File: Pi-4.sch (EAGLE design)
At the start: 14 parts, among them IC1 DS18B20, X1 RASPI_GPIO_B+#_PIN, X2 HDD, 5V 700mA, X3 MAC64L

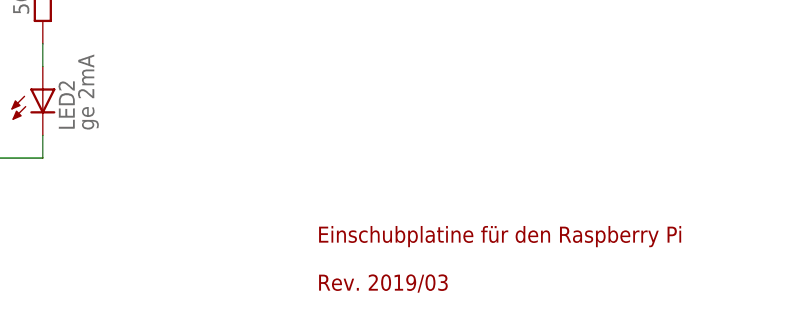
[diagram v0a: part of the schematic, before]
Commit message: Schaltpläne aufgehübscht zur Veröffentlichung
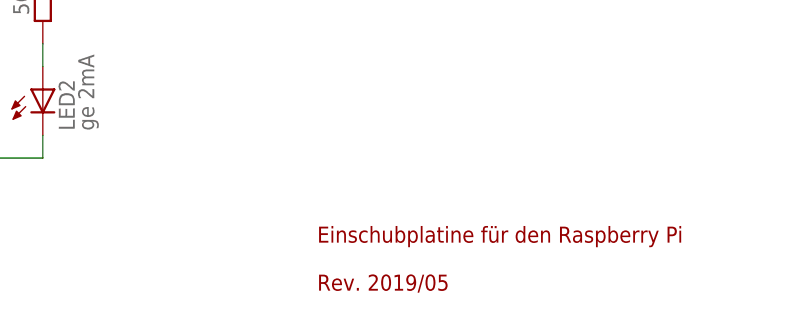
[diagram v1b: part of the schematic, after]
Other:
- note added: "Einschubplatine für den Raspberry Pi Rev. 2019/05"
- note removed: "Einschubplatine für den Raspberry Pi Rev. 2019/03"
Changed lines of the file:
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@@
 <plain>
 <text x="162.56" y="20.32" size="1.778" layer="94" align="top-left">Einschubplatine für den Raspberry Pi
-Rev. 2019/03</text>
+Rev. 2019/05</text>
 </plain>
 <instances>
